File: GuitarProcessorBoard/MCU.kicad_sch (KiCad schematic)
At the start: 92 parts, among them J301 SWD Header, J302 PWR, J303 TAP, J304 MODE, J305 BYP, J306 EXP, J307 ScopeGroundLoop, SW301 RST, SW302 BOOT, U301 STM32H7B0VBT6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

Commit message: routed & DRC passing
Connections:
- net LED_DATA: now also U301.54 (PB15); no longer U301.5 (PE6)
- net LED_LATCH: now also U301.51 (PB12); no longer U301.3 (PE4)
- net LED_NRST: now also U301.53 (PB14); no longer U301.4 (PE5)
- net LED_SCK: now also U301.52 (PB13); no longer U301.1 (PE2)
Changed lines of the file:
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@@
 	)
 	(no_connect
-		(at 160.274 141.224)
-	)
-	(no_connect
 		(at 160.274 166.624)
 	)
@@
 	)
 	(no_connect
+		(at 117.094 90.424)
+	)
+	(no_connect
 		(at 47.498 156.21)
 	)
@@
 	)
 	(no_connect
+		(at 117.094 98.044)
+	)
+	(no_connect
 		(at 117.094 110.744)
 	)
@@
 	)
 	(no_connect
-		(at 160.274 138.684)
+		(at 117.094 95.504)
 	)
 	(no_connect
@@
 	)
 	(no_connect
-		(at 160.274 136.144)
-	)
-	(no_connect
 		(at 117.094 153.924)
 	)
@@
 	)
 	(no_connect
+		(at 117.094 100.584)
+	)
+	(no_connect
 		(at 160.274 62.484)
 	)
@@
 	)
 	(no_connect
-		(at 160.274 143.764)
-	)
-	(no_connect
 		(at 117.094 133.604)
 	)
@@
 	(wire
 		(pts
-			(xy 114.046 100.584) (xy 117.094 100.584)
+			(xy 163.322 143.764) (xy 160.274 143.764)
 		)
 		(stroke
@@
 	(wire
 		(pts
-			(xy 114.046 95.504) (xy 117.094 95.504)
+			(xy 163.322 136.144) (xy 160.274 136.144)
 		)
 		(stroke
@@
 	(wire
 		(pts
-			(xy 114.046 90.424) (xy 117.094 90.424)
+			(xy 163.322 138.684) (xy 160.274 138.684)
 		)
 		(stroke
@@
 	(wire
 		(pts
-			(xy 114.046 98.044) (xy 117.094 98.044)
+			(xy 163.322 141.224) (xy 160.274 141.224)
 		)
 		(stroke
@@
 	(global_label "LED_LATCH"
 		(shape output)
-		(at 114.046 95.504 180)
+		(at 163.322 136.144 0)
 		(fields_autoplaced yes)
 		(effects
@@
 				(size 1.27 1.27)
 			)
-			(justify right)
+			(justify left)
 		)
 		(property "Intersheetrefs" "${INTERSHEET_REFS}"
-			(at 100.9613 95.504 0)
+			(at 176.4067 136.144 0)
 			(effects
 				(font
 					(size 1.27 1.27)
 				)
-				(justify right)
+				(justify left)
 				(hide yes)
 			)
@@
 	(global_label "LED_NRST"
 		(shape output)
-		(at 114.046 98.044 180)
+		(at 163.322 141.224 0)
 		(fields_autoplaced yes)
 		(effects
@@
 				(size 1.27 1.27)
 			)
-			(justify right)
+			(justify left)
 		)
 		(property "Intersheetrefs" "${INTERSHEET_REFS}"
-			(at 101.8685 98.044 0)
+			(at 175.4995 141.224 0)
 			(effects
 				(font
 					(size 1.27 1.27)
 				)
-				(justify right)
+				(justify left)
 				(hide yes)
 			)
@@
 	(global_label "LED_DATA"
 		(shape output)
-		(at 114.046 100.584 180)
+		(at 163.322 143.764 0)
 		(fields_autoplaced yes)
 		(effects
@@
 				(size 1.27 1.27)
 			)
-			(justify right)
+			(justify left)
 		)
 		(property "Intersheetrefs" "${INTERSHEET_REFS}"
-			(at 102.2313 100.584 0)
+			(at 175.1367 143.764 0)
 			(effects
 				(font
 					(size 1.27 1.27)
 				)
-				(justify right)
+				(justify left)
 				(hide yes)
 			)
@@
 	(global_label "LED_SCK"
 		(shape output)
-		(at 114.046 90.424 180)
+		(at 163.322 138.684 0)
 		(fields_autoplaced yes)
 		(effects
@@
 				(size 1.27 1.27)
 			)
-			(justify right)
+			(justify left)
 		)
 		(property "Intersheetrefs" "${INTERSHEET_REFS}"
-			(at 102.8966 90.424 0)
+			(at 174.4714 138.684 0)
 			(effects
 				(font
 					(size 1.27 1.27)
 				)
-				(justify right)
+				(justify left)
 				(hide yes)
 			)

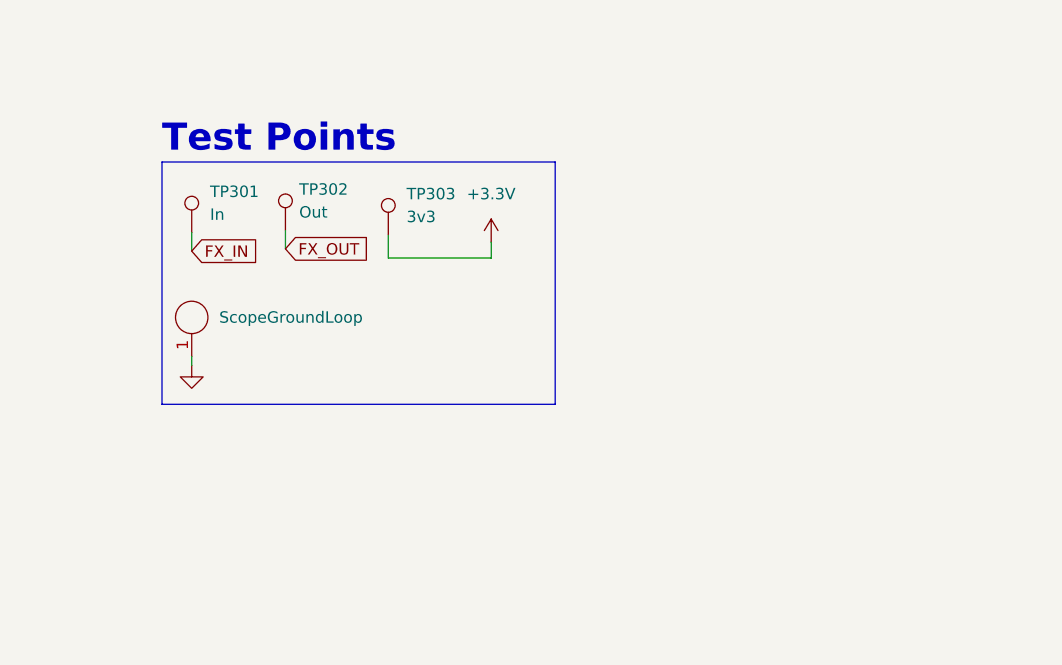
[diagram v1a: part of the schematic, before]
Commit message: more test points, trace clean up
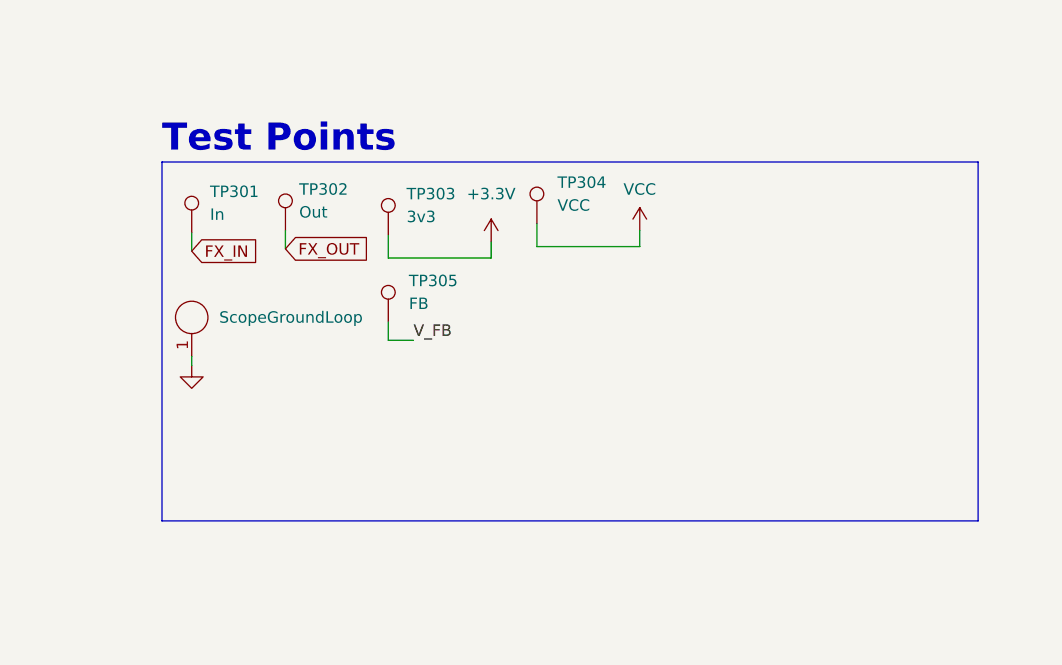
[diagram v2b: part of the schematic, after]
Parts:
- added TP304: VCC, TestPoint:TestPoint_THTPad_D2.0mm_Drill1.0mm_VAL, symbol Connector:TestPoint
- added TP305: FB, TestPoint:TestPoint_THTPad_D2.0mm_Drill1.0mm_VAL, symbol Connector:TestPoint
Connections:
- net VCC: now also TP304.1
- net V_FB: now also TP305.1

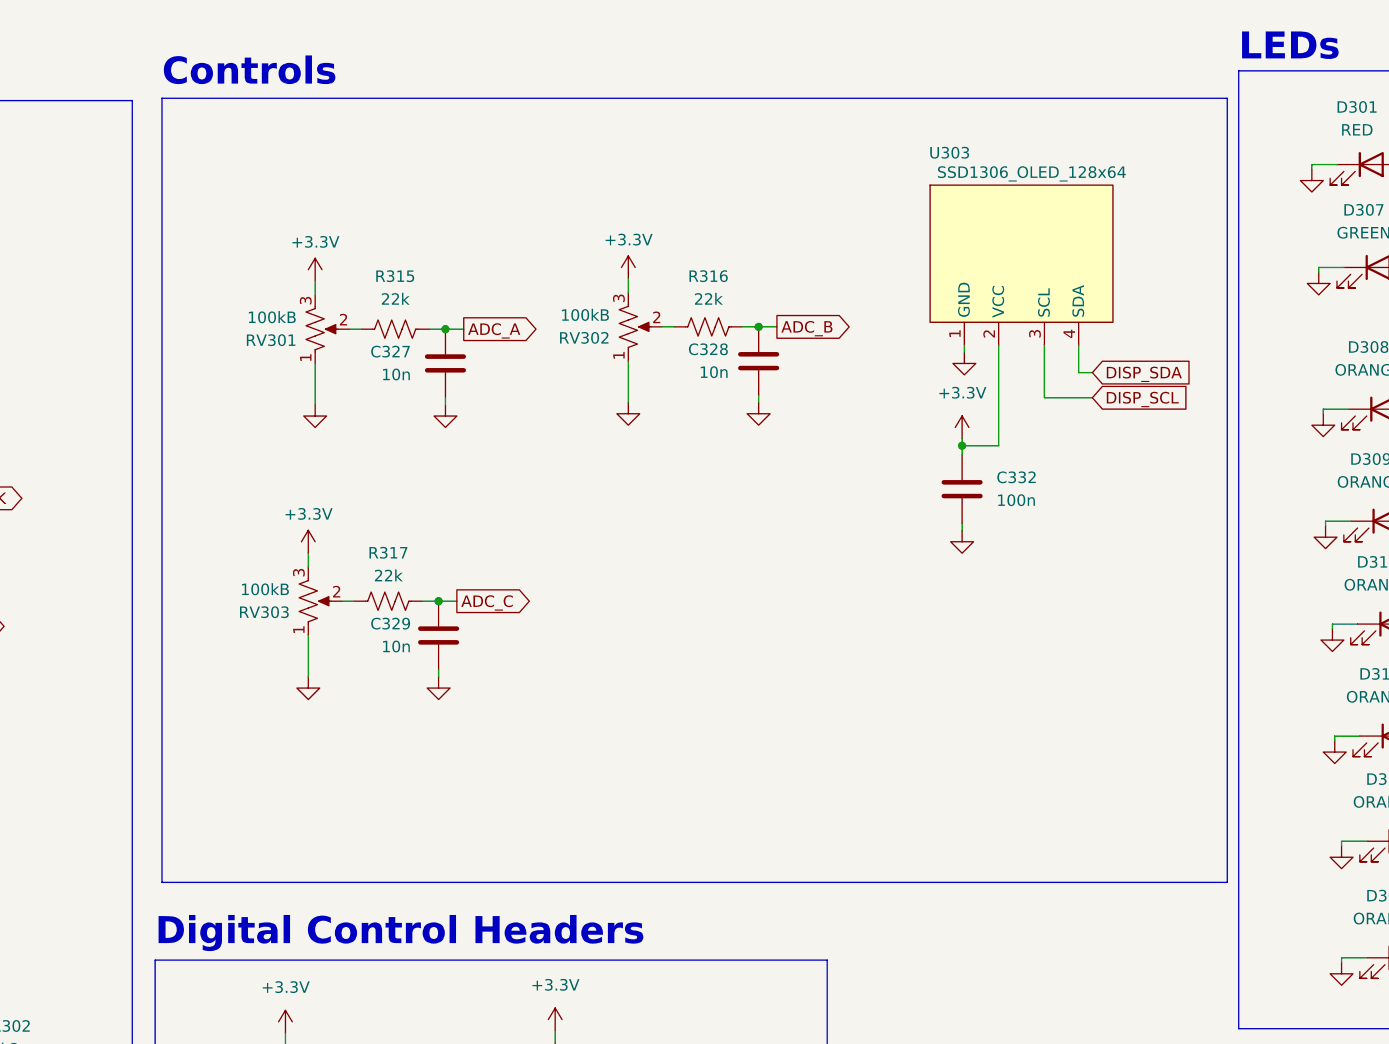
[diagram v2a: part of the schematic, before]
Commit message: processing callback set up
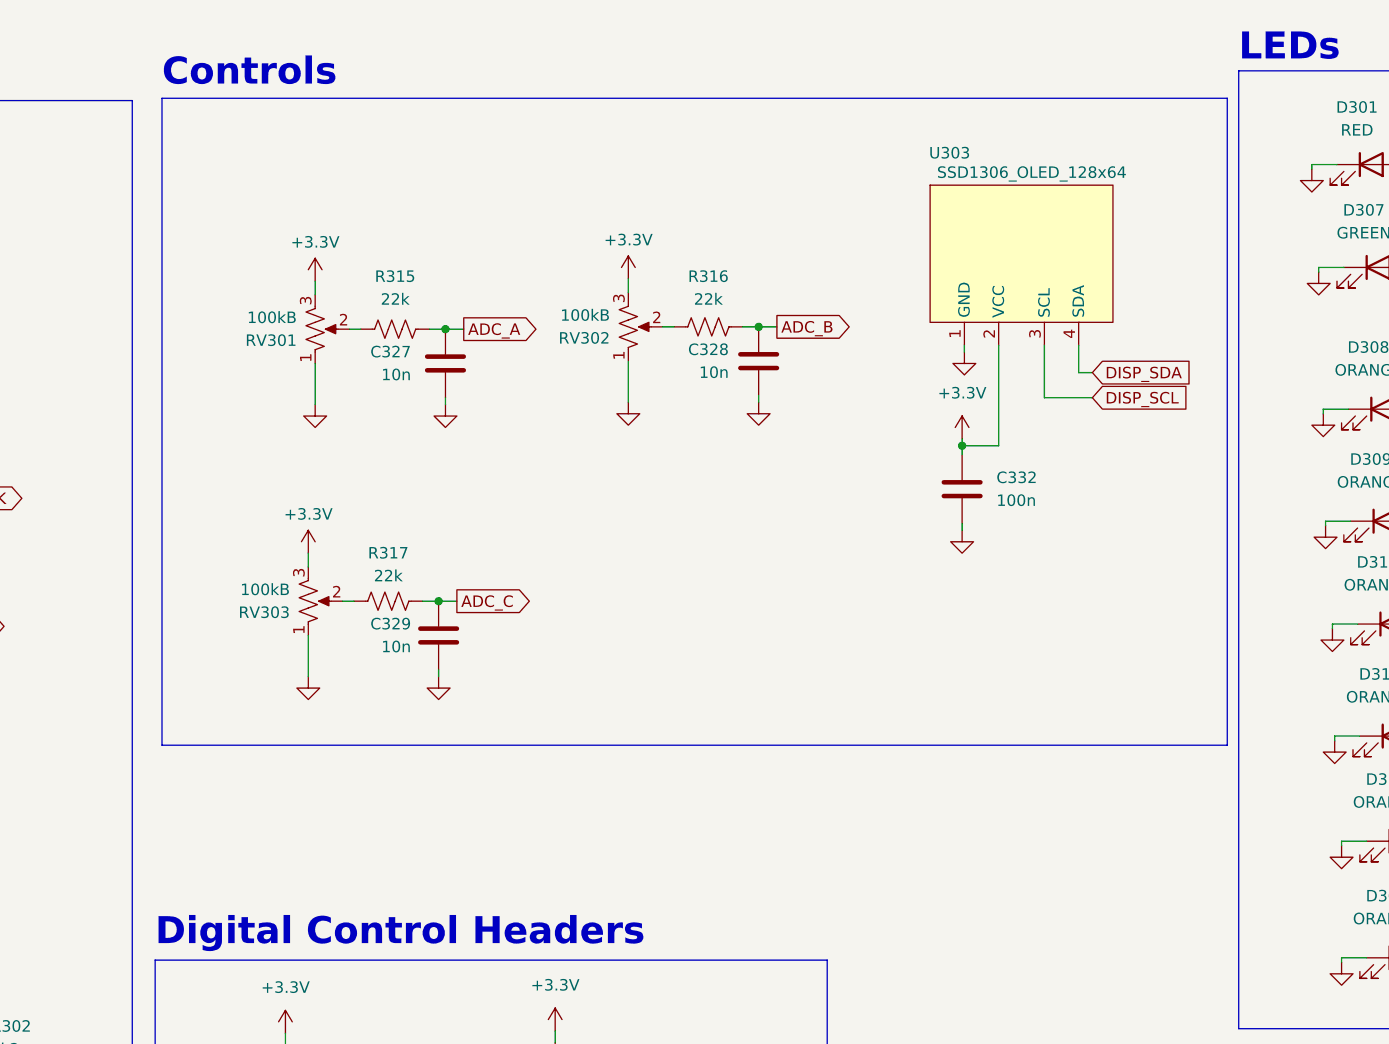
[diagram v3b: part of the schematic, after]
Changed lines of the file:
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@@
 	(rectangle
 		(start 232.664 21.59)
-		(end 351.028 108.712)
+		(end 351.028 93.472)
 		(stroke
 			(width 0)

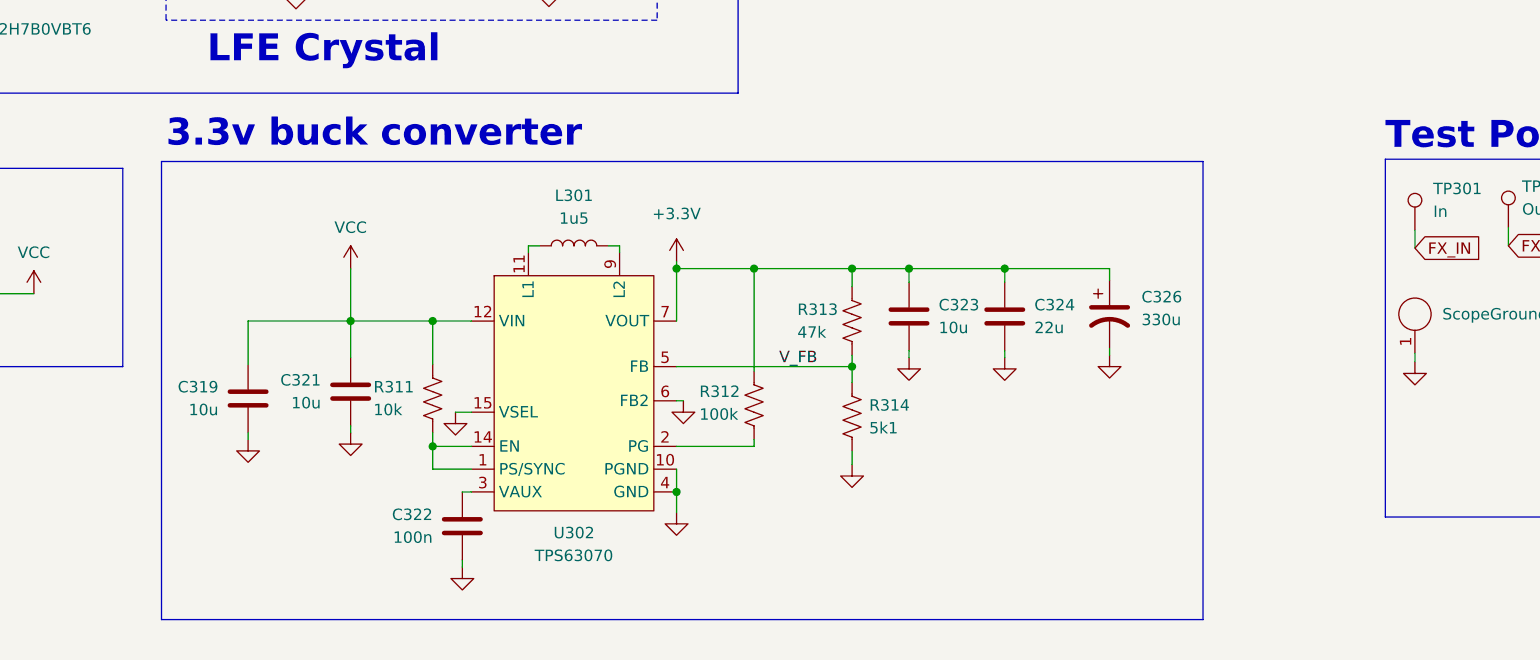
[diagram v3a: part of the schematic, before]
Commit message: differential output stage
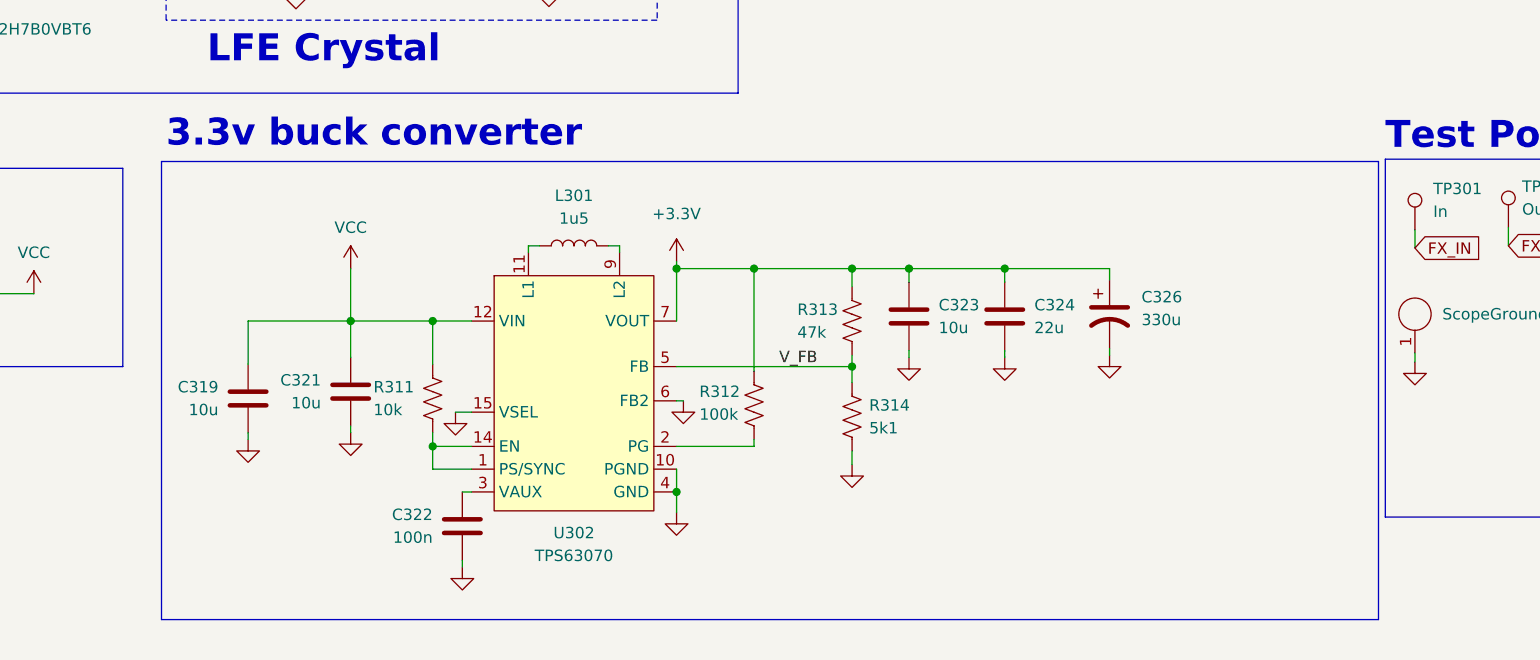
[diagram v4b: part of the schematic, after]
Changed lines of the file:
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@@
 	(rectangle
 		(start 165.1 211.074)
-		(end 281.178 262.128)
+		(end 300.736 262.128)
 		(stroke
 			(width 0)
